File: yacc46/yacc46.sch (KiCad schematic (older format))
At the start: 125 parts, among them J1 OLED_I2C, J2 GLOVE_I2C, SW1 SW_PUSH, SW10 SW_PUSH, SW11 SW_PUSH, SW12 SW_PUSH, SW13 SW_PUSH, SW14 SW_PUSH, SW15 SW_PUSH, SW16 SW_PUSH, SW17 SW_PUSH, SW18 SW_PUSH, SW19 Rotary_Encoder_Switch, SW2 SW_PUSH, SW20 SW_PUSH, SW21 SW_PUSH, SW22 SW_PUSH, SW23 SW_PUSH, SW24 SW_PUSH, SW25 SW_PUSH, SW26 SW_PUSH, SW27 SW_PUSH, SW28 SW_PUSH, SW29 SW_PUSH, SW3 SW_PUSH, SW30 SW_PUSH, SW31 SW_PUSH, SW32 SW_PUSH, SW33 SW_PUSH, SW34 SW_PUSH, SW35 SW_PUSH, SW36 Rotary_Encoder_Switch, SW37 SW_PUSH, SW38 SW_PUSH, SW39 SW_PUSH, SW4 SW_PUSH, SW40 SW_PUSH, SW41 SW_PUSH, SW42 SW_PUSH, SW43 SW_PUSH, SW44 SW_PUSH, SW45 SW_PUSH, SW46 SW_PUSH, SW47 SW_Push, SW5 SW_PUSH, SW6 SW_PUSH, SW7 SW_PUSH, SW8 SW_PUSH, SW9 SW_PUSH, U1 ProMicro_r

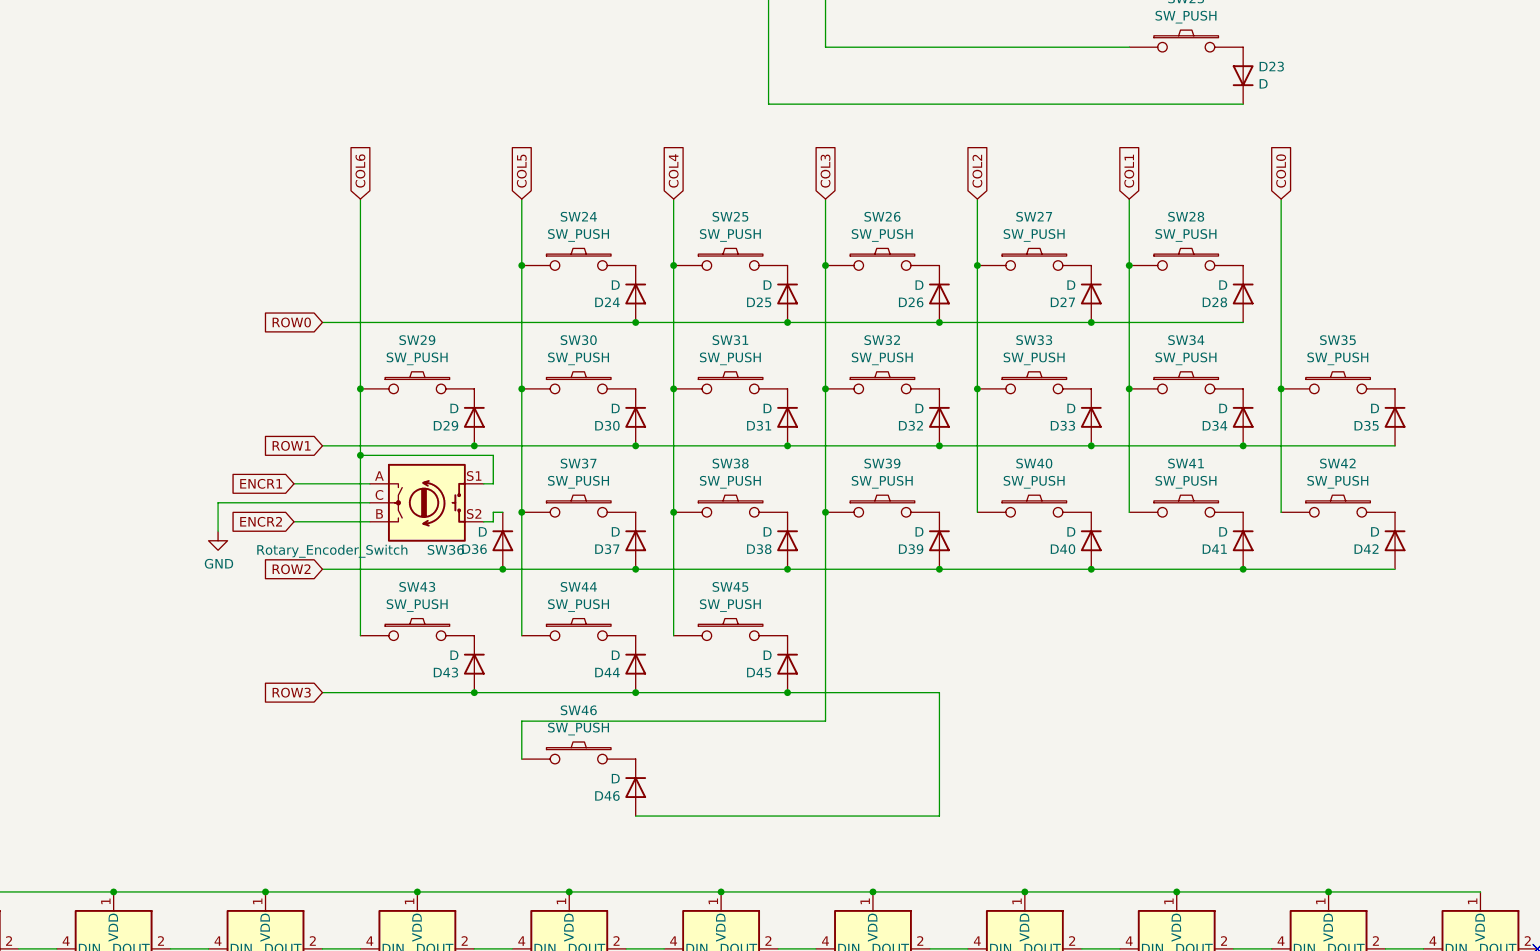
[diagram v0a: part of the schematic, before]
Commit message: flip right hand side's diodes direction
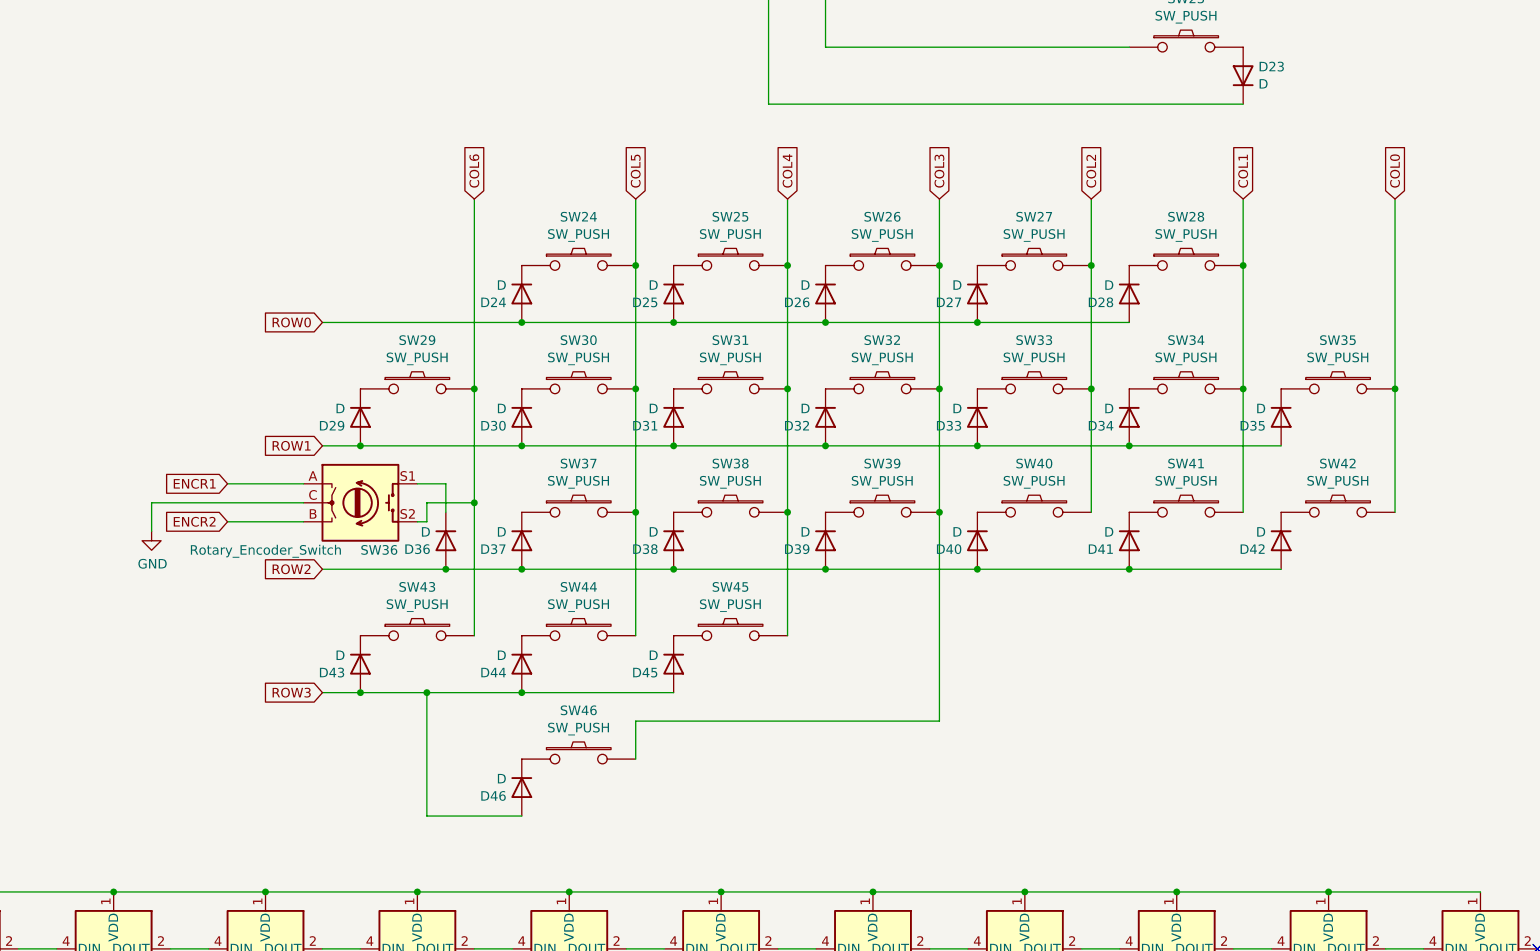
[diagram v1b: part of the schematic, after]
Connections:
- wire segments 184 -> 183
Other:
- moved on the sheet: D24, D25, D26, D27, D28, D29, D30, D31, D32, D33, D34, D35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

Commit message: modify PCB design rules
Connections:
- net labels added: LED_POWER
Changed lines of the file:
@@
 L power:VCC #PWR019
 U 1 1 5FB87C1E
-P 900 8200
-F 0 "#PWR019" H 900 8050 50  0001 C CNN
-F 1 "VCC" H 915 8373 50  0000 C CNN
-F 2 "" H 900 8200 50  0001 C CNN
-F 3 "" H 900 8200 50  0001 C CNN
-	1    900  8200
+P 900 8050
+F 0 "#PWR019" H 900 7900 50  0001 C CNN
+F 1 "VCC" H 915 8223 50  0000 C CNN
+F 2 "" H 900 8050 50  0001 C CNN
+F 3 "" H 900 8050 50  0001 C CNN
+	1    900  8050
 	1    0    0    -1
 $EndComp
@@
 L Jumper:SolderJumper_3_Open JP1
 U 1 1 614ABBD0
-P 1250 8200
-F 0 "JP1" H 1250 8405 50  0000 C CNN
-F 1 "SolderJumper_3_Open" H 1407 8314 50  0000 C CNN
-F 2 "Jumper:SolderJumper-3_P2.0mm_Open_TrianglePad1.0x1.5mm" H 1250 8200 50  0001 C CNN
-F 3 "~" H 1250 8200 50  0001 C CNN
-	1    1250 8200
+P 1250 8050
+F 0 "JP1" H 1250 8255 50  0000 C CNN
+F 1 "SolderJumper_3_Open" H 1407 8164 50  0000 C CNN
+F 2 "Jumper:SolderJumper-3_P2.0mm_Open_TrianglePad1.0x1.5mm" H 1250 8050 50  0001 C CNN
+F 3 "~" H 1250 8050 50  0001 C CNN
+	1    1250 8050
 	1    0    0    -1
 $EndComp
 Text GLabel 2450 1150 0    50   Input ~ 0
 RAW
-Text GLabel 1450 8200 2    50   Input ~ 0
+Text GLabel 1450 8050 2    50   Input ~ 0
 RAW
 Wire Wire Line
-	1250 8350 1250 8500
-Wire Wire Line
 	1250 8500 1400 8500
 Wire Wire Line
-	900  8200 1050 8200
+	900  8050 1050 8050
 Wire Wire Line
 	5400 8500 6200 8500
@@
 Wire Wire Line
 	6500 6450 6500 7150
+Wire Wire Line
+	1250 8200 1250 8500
+Text Label 1250 8400 0    50   ~ 0
+LED_POWER
 $EndSCHEMATC

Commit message: wire PCB
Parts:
- SW19, SW36: footprint 1m38_kbd:RotaryEncoder_Alps_EC11E-and-CherryMX-Single -> 1m38_kbd:RotaryEncoder_Alps_EC11E-and-CherryMX-Hotswap
- U1: footprint foostan_kbd:ProMicro_v3 -> 1m38_kbd:ProMicro
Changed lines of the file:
@@
 F 0 "SW19" H 11250 3000 50  0000 L CNN
 F 1 "Rotary_Encoder_Switch" H 10650 3100 50  0000 L CNN
-F 2 "1m38_kbd:RotaryEncoder_Alps_EC11E-and-CherryMX-Single" H 11300 2910 50  0001 C CNN
+F 2 "1m38_kbd:RotaryEncoder_Alps_EC11E-and-CherryMX-Hotswap" H 11300 2910 50  0001 C CNN
 F 3 "~" H 11450 3010 50  0001 C CNN
 	1    11450 2750
@@
 F 0 "SW36" H 5900 6200 50  0000 L CNN
 F 1 "Rotary_Encoder_Switch" H 5000 6200 50  0000 L CNN
-F 2 "1m38_kbd:RotaryEncoder_Alps_EC11E-and-CherryMX-Single" H 5750 6610 50  0001 C CNN
+F 2 "1m38_kbd:RotaryEncoder_Alps_EC11E-and-CherryMX-Hotswap" H 5750 6610 50  0001 C CNN
 F 3 "~" H 5900 6710 50  0001 C CNN
 	1    5900 6450
@@
 F 0 "U1" H 3150 2837 60  0000 C CNN
 F 1 "ProMicro_r" H 3150 2731 60  0000 C CNN
-F 2 "foostan_kbd:ProMicro_v3" H 3250 800 60  0001 C CNN
+F 2 "1m38_kbd:ProMicro" H 3250 800 60  0001 C CNN
 F 3 "" H 3250 800 60  0000 C CNN
 	1    3100 1850

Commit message: move cover-plate screw hole
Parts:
- U1: footprint 1m38_kbd:ProMicro -> foostan_kbd:ProMicro_v3
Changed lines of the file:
@@
 F 0 "U1" H 3150 2837 60  0000 C CNN
 F 1 "ProMicro_r" H 3150 2731 60  0000 C CNN
-F 2 "1m38_kbd:ProMicro" H 3250 800 60  0001 C CNN
+F 2 "foostan_kbd:ProMicro_v3" H 3250 800 60  0001 C CNN
 F 3 "" H 3250 800 60  0000 C CNN
 	1    3100 1850
